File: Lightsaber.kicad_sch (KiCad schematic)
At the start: 32 parts, among them J1 Neopixel LEDs, J2 USB_B_Micro, M1 Motor_DC, Q1 2N2222, Q2 2N3904, Q3 2N3904, SW1 SW_Push, SW2 SW_DIP_x01, U1 PAM8403D, U2 MPU-6050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

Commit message: added test points and footprints
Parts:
- added TP1, TP2, TP3, TP4, TP5, TP6, TP7, TP8, TP9: TestPoint, Connector_PinHeader_1.00mm:PinHeader_1x01_P1.00mm_Vertical, symbol Connector:TestPoint
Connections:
- net +9V: now also TP1.1, TP9.1
- net at C4.1, J1.3 (Pin_3), R2.1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: now also TP3.1
- net at J1.2 (Pin_2), Q2.3 (C), R2.2: now also TP4.1
- net at C7.1, U5.2 (3V3), U6.5 (OUT): now also TP8.1
- net at R6.1, U5.6 (GPIO6/TOUCH6/ADC1_CH5): now also TP5.1
- net at R5.2, U5.7 (GPIO7/TOUCH7/ADC1_CH6): now also TP2.1
- net at LS1.1, U1.1 (LOUT+): now also TP6.1
- net at RV1.2, U1.7 (INL): now also TP7.1

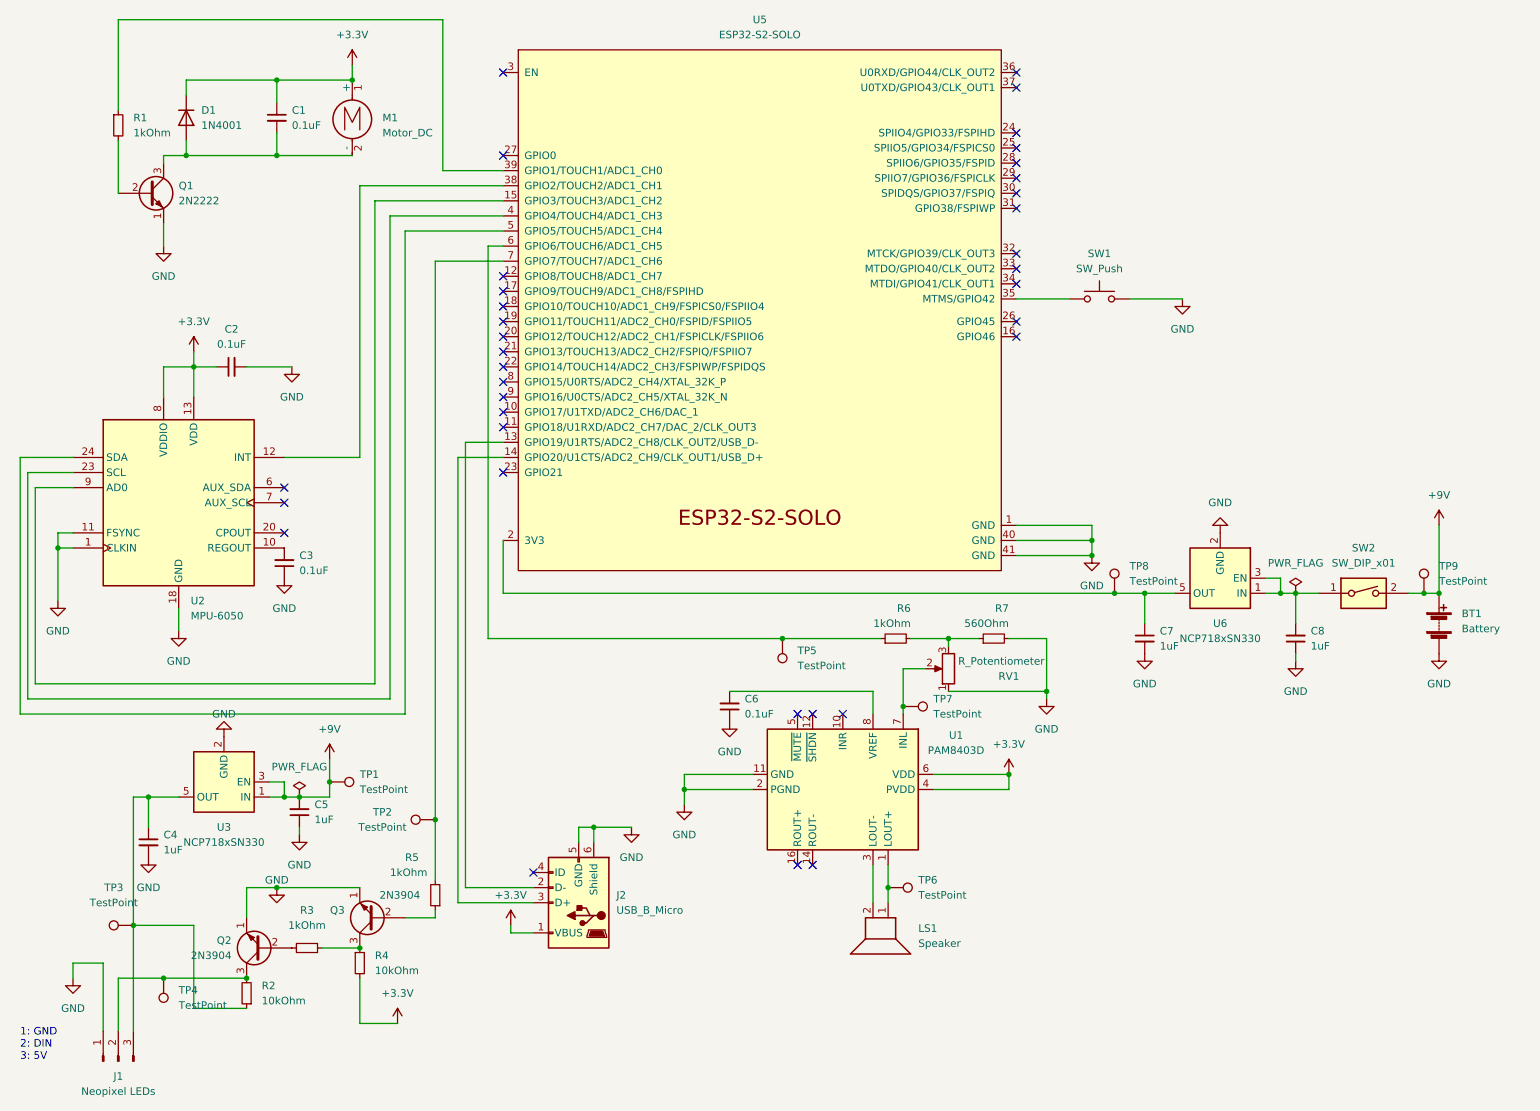
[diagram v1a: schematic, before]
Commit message: thickened power traces, fixed all errors, placed test points on layout
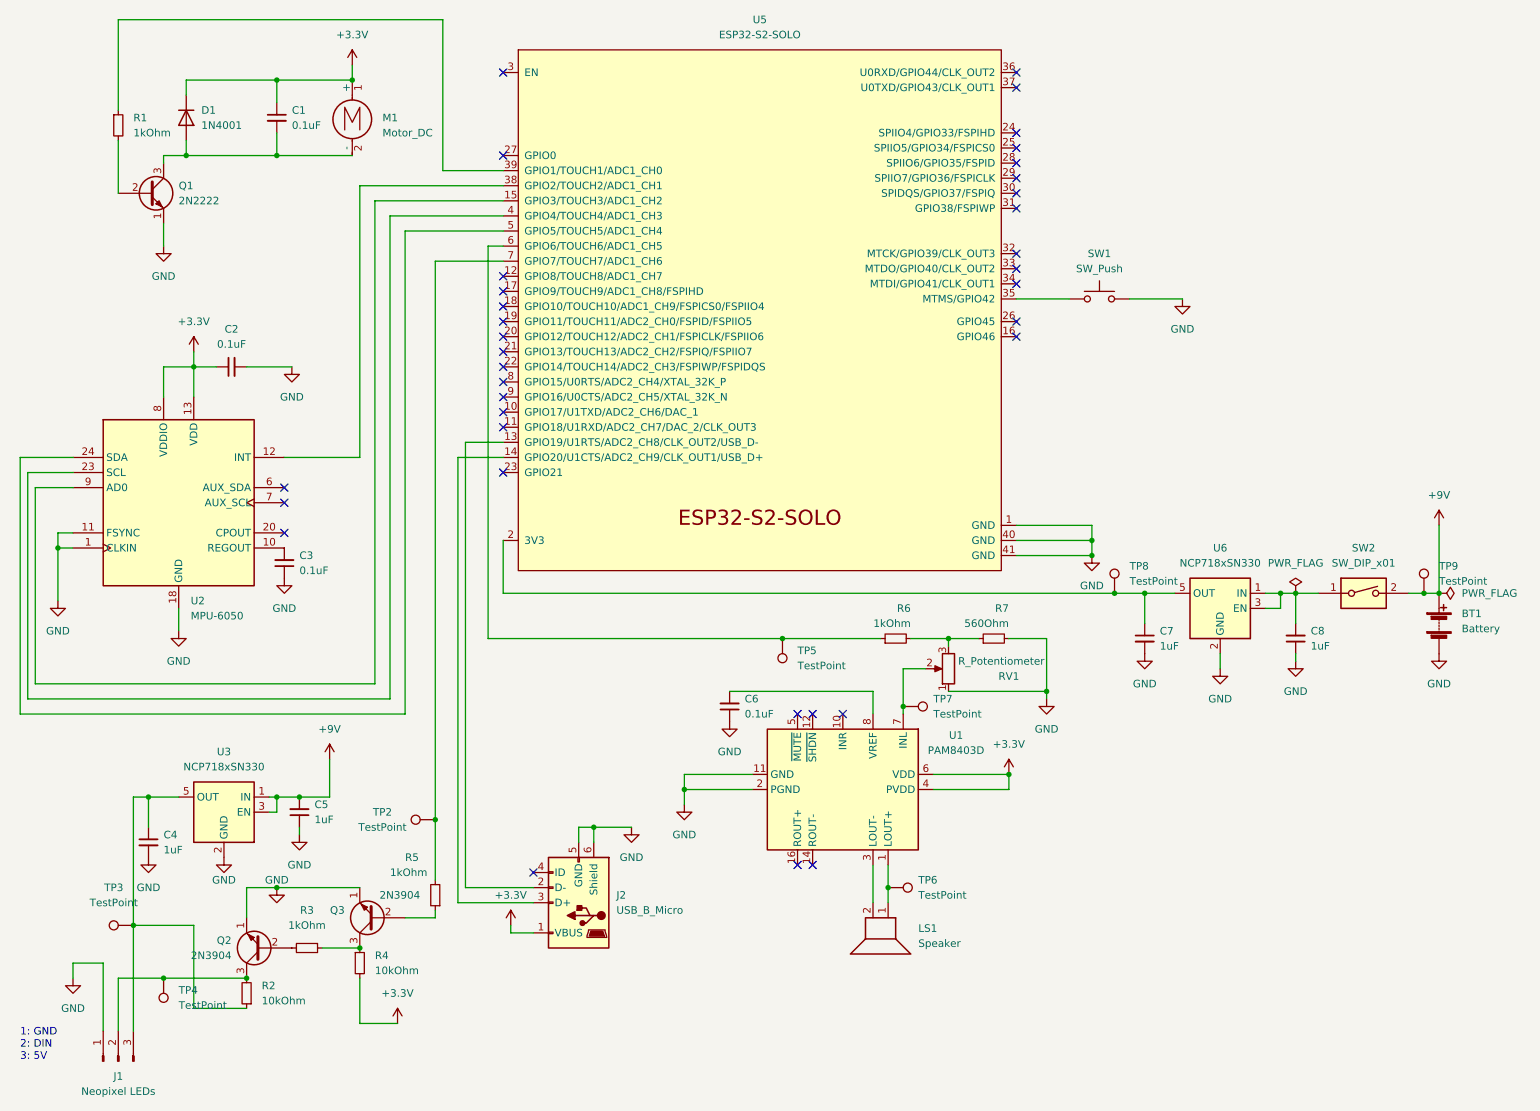
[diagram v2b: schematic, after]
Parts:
- removed TP1: TestPoint, Connector_PinHeader_1.00mm:PinHeader_1x01_P1.00mm_Vertical, symbol Connector:TestPoint
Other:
- moved on the sheet: U3, U6

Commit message: finished
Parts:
- removed C2, C3: 0.1uF, Capacitor_SMD:C_0201_0603Metric, symbol Device:C_Small
- removed U2: MPU-6050, Sensor_Motion:InvenSense_QFN-24_4x4mm_P0.5mm, symbol Sensor_Motion:MPU-6050
- added J3: Conn_01x05_Female, Connector_PinSocket_2.54mm:PinSocket_1x05_P2.54mm_Vertical, symbol Connector:Conn_01x05_Female
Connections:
- net +3.3V: now also J3.5 (Pin_5)
- net GND: now also J3.4 (Pin_4)
- net at R5.2, TP2.1: no longer U5.7 (GPIO7/TOUCH7/ADC1_CH6)
- net at U5.15 (GPIO3/TOUCH3/ADC1_CH2): now also J3.2 (Pin_2)
- net at U5.38 (GPIO2/TOUCH2/ADC1_CH1): now also J3.1 (Pin_1)
- net at U5.4 (GPIO4/TOUCH4/ADC1_CH3): now also J3.3 (Pin_3)
- no-connect marks 36 -> 35
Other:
- note added: "1: VCC 2: GND 3: SCL 4: SDA 5: INT"
